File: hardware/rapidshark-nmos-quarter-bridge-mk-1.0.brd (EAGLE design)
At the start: 20.3 x 30.5 mm, 12 parts, among them Q1 STP60NF06L

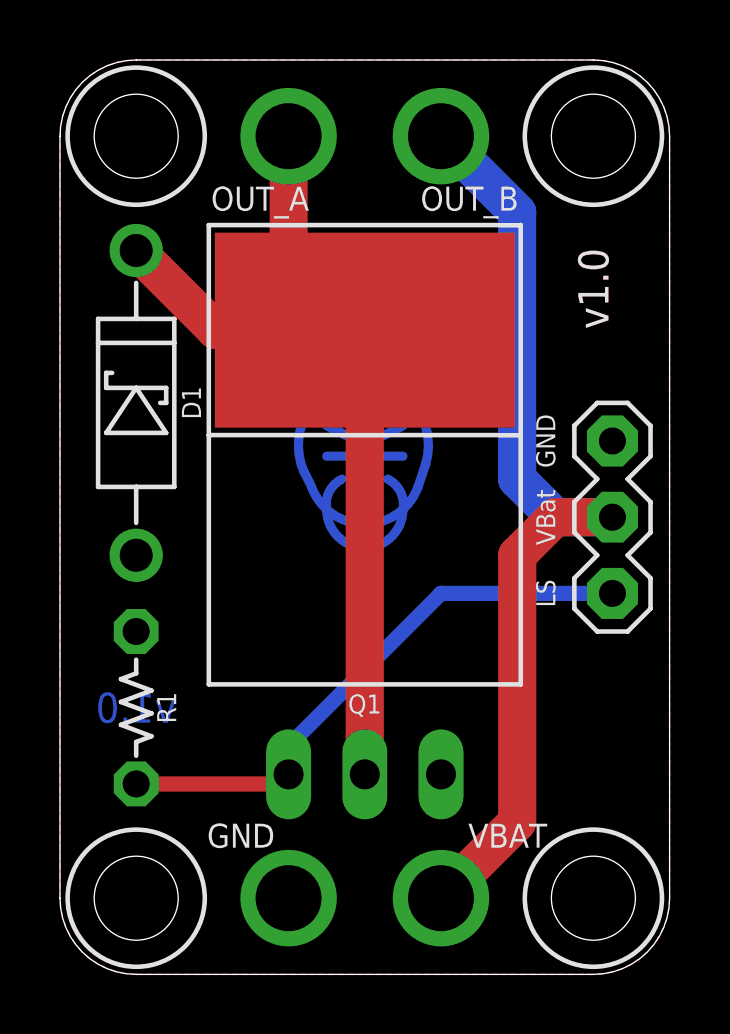
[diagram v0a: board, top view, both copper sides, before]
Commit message: silkscreen changes
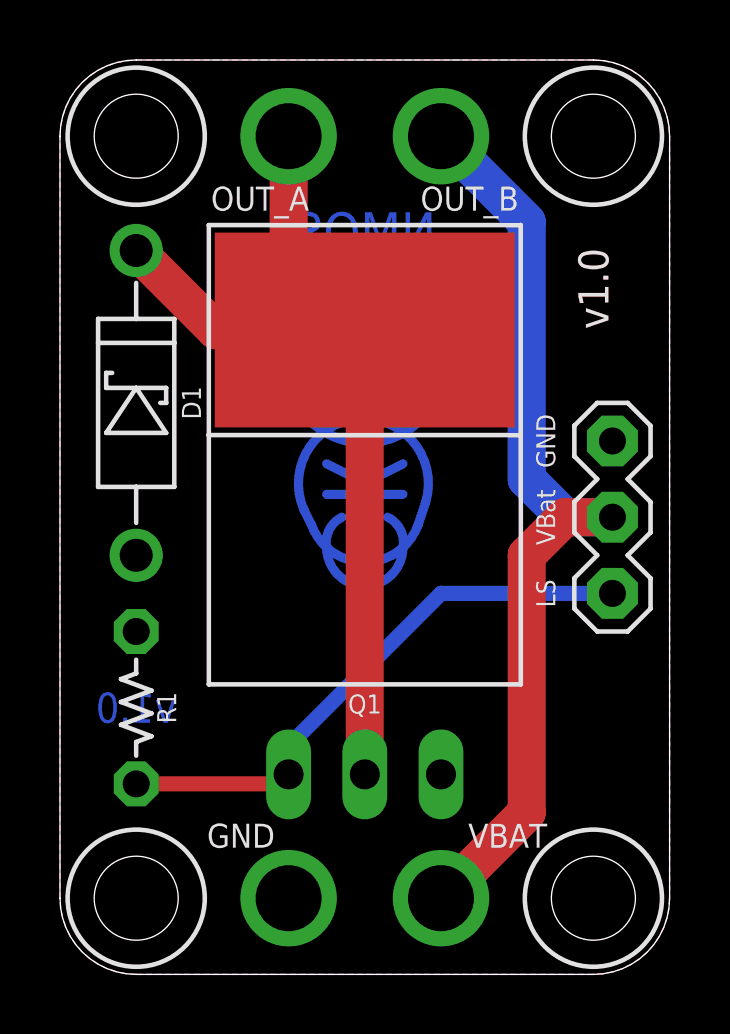
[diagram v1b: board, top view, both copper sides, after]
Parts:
- moved U$1 1.27 mm to (10.2, 16.5)
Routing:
- added copper zone on layer 16, net GND
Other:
- board text added: "NMOS Quarter Bridge"
- board text removed: "Quarter Bridge"
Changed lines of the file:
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@@
 <circle x="2.54" y="2.54" radius="2.286" width="0.1524" layer="21"/>
 <circle x="17.78" y="2.54" radius="2.286" width="0.1524" layer="21"/>
-<text x="10.16" y="22.86" size="1.27" layer="22" font="vector" ratio="12" rot="MR0" align="center">Quarter
+<text x="10.16" y="22.86" size="1.27" layer="22" font="vector" ratio="12" rot="MR0" align="center">NMOS
+Quarter
 Bridge</text>
-<text x="10.16" y="11.43" size="1" layer="22" font="vector" ratio="12" rot="MR0" align="center">by schizobovine
+<text x="10.16" y="10.16" size="1" layer="22" font="vector" ratio="12" rot="MR0" align="center">by schizobovine
 &lt;sean@yak.net&gt;</text>
-<text x="10.16" y="22.86" size="1.27" layer="16" font="vector" ratio="12" rot="MR0" align="center">Quarter
+<text x="10.16" y="22.86" size="1.27" layer="16" font="vector" ratio="12" rot="MR0" align="center">NMOS
+Quarter
 Bridge</text>
 <text x="17.78" y="22.86" size="1" layer="21" font="vector" ratio="16" rot="R90" align="center">v1.0</text>
@@
 <attribute name="VALUE" x="1.8415" y="8.89" size="0.635" layer="27" font="vector" ratio="12" rot="R270" align="top-center"/>
 </element>
-<element name="U$1" library="a_parts" package="COW_SMALL_METAL_NOTEXT" value="" x="10.16" y="17.78" rot="MR0"/>
+<element name="U$1" library="a_parts" package="COW_SMALL_METAL_NOTEXT" value="" x="10.16" y="16.51" rot="MR0"/>
 <element name="U$2" library="a_parts" package="CC-BY-SA-4.0-NO-URL" value="" x="16.8275" y="6.6675" rot="MR0"/>
 <element name="U$3" library="a_parts" package="OSHWLOGO_TINY_SILKONLY" value="" x="5.08" y="6.35" rot="MR0"/>
@@
 <contactref element="R1" pad="P$1"/>
 <contactref element="JP1" pad="1"/>
+<polygon width="0.1524" layer="16" isolate="0.3048" rank="5">
+<vertex x="17.78" y="0"/>
+<vertex x="2.54" y="0" curve="-90"/>
+<vertex x="0" y="2.54"/>
+<vertex x="0" y="27.94" curve="-90"/>
+<vertex x="2.54" y="30.48"/>
+<vertex x="17.78" y="30.48" curve="-90"/>
+<vertex x="20.32" y="27.94"/>
+<vertex x="20.32" y="2.54" curve="-90"/>
+</polygon>
 </signal>
 <signal name="V_BATT">
@@
 <contactref element="OUT_B" pad="1"/>
 <contactref element="JP1" pad="2"/>
-<wire x1="12.7" y1="2.54" x2="15.24" y2="5.08" width="1.27" layer="1"/>
-<wire x1="15.24" y1="5.08" x2="15.24" y2="13.97" width="1.27" layer="1"/>
-<wire x1="15.24" y1="13.97" x2="16.51" y2="15.24" width="1.27" layer="1"/>
-<wire x1="16.51" y1="15.24" x2="18.415" y2="15.24" width="1.27" layer="1"/>
-<wire x1="12.7" y1="27.94" x2="15.24" y2="25.4" width="1.27" layer="16"/>
-<wire x1="15.24" y1="25.4" x2="15.24" y2="16.51" width="1.27" layer="16"/>
-<wire x1="15.24" y1="16.51" x2="16.51" y2="15.24" width="1.27" layer="16"/>
-<wire x1="16.51" y1="15.24" x2="18.415" y2="15.24" width="1.27" layer="16"/>
+<wire x1="12.7" y1="2.54" x2="15.5575" y2="5.3975" width="1.27" layer="1"/>
+<wire x1="15.5575" y1="5.3975" x2="15.5575" y2="13.97" width="1.27" layer="1"/>
+<wire x1="15.5575" y1="13.97" x2="16.8275" y2="15.24" width="1.27" layer="1"/>
+<wire x1="16.8275" y1="15.24" x2="18.415" y2="15.24" width="1.27" layer="1"/>
+<wire x1="12.7" y1="27.94" x2="15.5575" y2="25.0825" width="1.27" layer="16"/>
+<wire x1="15.5575" y1="25.0825" x2="15.5575" y2="16.51" width="1.27" layer="16"/>
+<wire x1="15.5575" y1="16.51" x2="16.8275" y2="15.24" width="1.27" layer="16"/>
+<wire x1="16.8275" y1="15.24" x2="18.415" y2="15.24" width="1.27" layer="16"/>
 </signal>
 <signal name="A">
